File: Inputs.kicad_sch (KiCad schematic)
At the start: 6 parts, among them J23 Conn_01x04_Socket, J24 Conn_01x04_Socket, J25 Conn_01x04_Socket, J26 Conn_01x04_Socket, J27 Conn_01x02_Socket

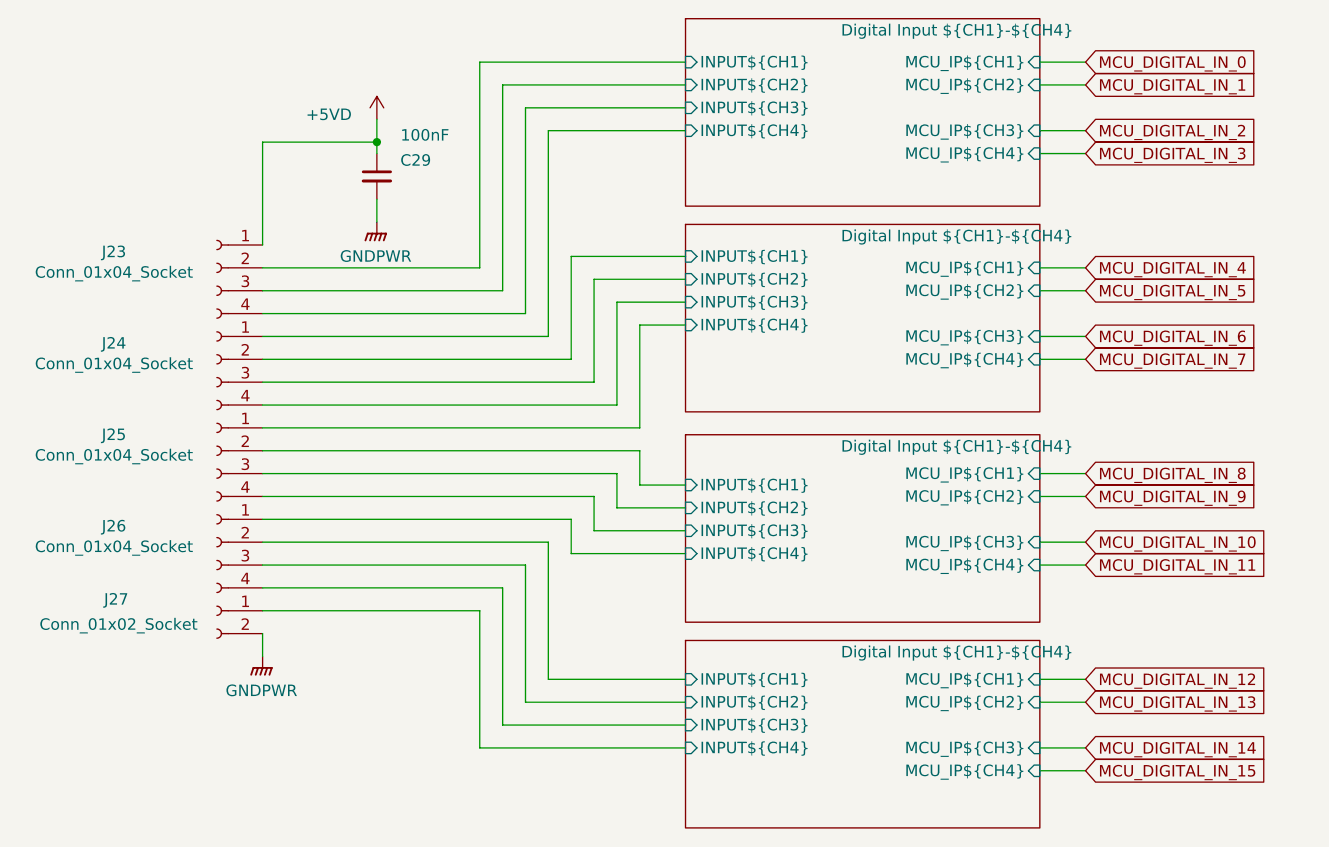
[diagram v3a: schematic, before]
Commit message: Added Analog inputs, updates to readme re powering board from external supply
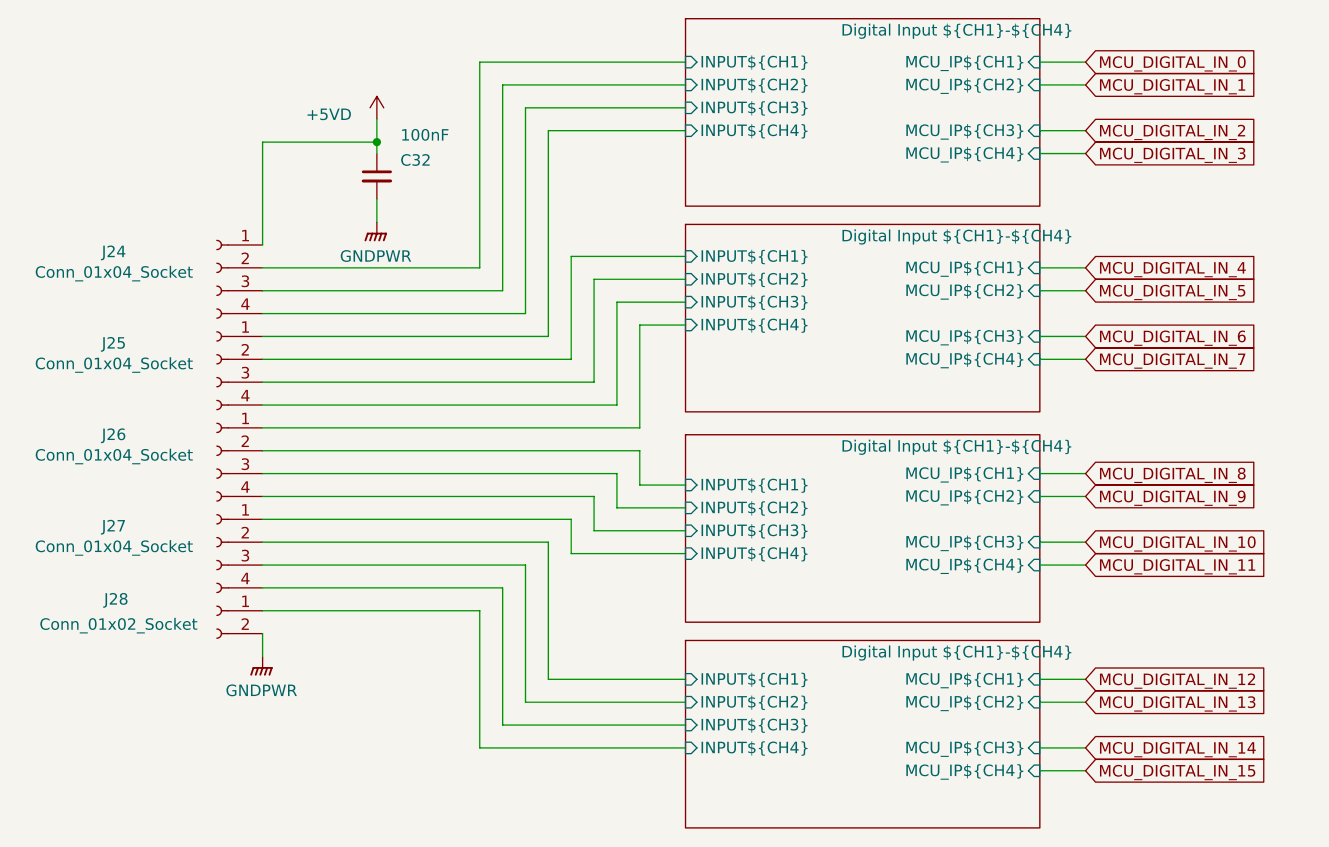
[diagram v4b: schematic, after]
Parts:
- renumbered C29 to C32, J23 to J24, J24 to J25, J25 to J26, J26 to J27, J27 to J28
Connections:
- net Digital Input ${CH1}-${CH4}/INPUT${CH1} is gone; now on net Digital Input ${CH1}-${CH4}/INPUT${CH1}: J25.2 (Pin_2)
- net Digital Input ${CH1}-${CH4}/INPUT${CH2} is gone; now on net Digital Input ${CH1}-${CH4}/INPUT${CH2}: J25.3 (Pin_3)
- net Digital Input ${CH1}-${CH4}/INPUT${CH3} is gone; now on net Digital Input ${CH1}-${CH4}/INPUT${CH3}: J25.4 (Pin_4)
- net Digital Input ${CH1}-${CH4}/INPUT${CH4} is gone; now on net Digital Input ${CH1}-${CH4}/INPUT${CH4}: J25.1 (Pin_1)
- net Digital Input ${CH1}-${CH4}/INPUT${CH1}: no longer J27.2 (Pin_2)
- net Digital Input ${CH1}-${CH4}/INPUT${CH2}: no longer J27.3 (Pin_3)
- net Digital Input ${CH1}-${CH4}/INPUT${CH3}: no longer J27.4 (Pin_4)
- net Digital Input ${CH1}-${CH4}/INPUT${CH4}: no longer J27.1 (Pin_1)
- new net Digital Input ${CH1}-${CH4}/INPUT${CH1}: J27.2 (Pin_2)
- new net Digital Input ${CH1}-${CH4}/INPUT${CH2}: J27.3 (Pin_3)
- new net Digital Input ${CH1}-${CH4}/INPUT${CH3}: J27.4 (Pin_4)
- new net Digital Input ${CH1}-${CH4}/INPUT${CH4}: J27.1 (Pin_1)
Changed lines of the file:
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@@
 		(on_board yes)
 		(dnp no)
-		(property "Reference" "J26"
+		(property "Reference" "J27"
 			(at 80.01 104.902 0)
 			(effects
@@
 			(project "Remora Nucleo F446ZE Hat"
 				(path "/5473abc6-7b93-43cc-a401-f691c4d7d7cf/181d5939-8311-41b3-8216-f7233e3a75eb"
-					(reference "J26")
+					(reference "J27")
 					(unit 1)
 				)
@@
 		(dnp no)
 		(fields_autoplaced yes)
-		(property "Reference" "#PWR0202"
+		(property "Reference" "#PWR0211"
 			(at 96.52 124.46 0)
 			(effects
@@
 			(project "Remora Nucleo F446ZE Hat"
 				(path "/5473abc6-7b93-43cc-a401-f691c4d7d7cf/181d5939-8311-41b3-8216-f7233e3a75eb"
-					(reference "#PWR0202")
+					(reference "#PWR0211")
 					(unit 1)
 				)
@@
 		(on_board yes)
 		(dnp no)
-		(property "Reference" "#PWR0203"
+		(property "Reference" "#PWR0212"
 			(at 109.22 63.5 0)
 			(effects
@@
 			(project "Remora Nucleo F446ZE Hat"
 				(path "/5473abc6-7b93-43cc-a401-f691c4d7d7cf/181d5939-8311-41b3-8216-f7233e3a75eb"
-					(reference "#PWR0203")
+					(reference "#PWR0212")
 					(unit 1)
 				)
@@
 		(on_board yes)
 		(dnp no)
-		(property "Reference" "J23"
+		(property "Reference" "J24"
 			(at 80.01 74.422 0)
 			(effects
@@
 			(project "Remora Nucleo F446ZE Hat"
 				(path "/5473abc6-7b93-43cc-a401-f691c4d7d7cf/181d5939-8311-41b3-8216-f7233e3a75eb"
-					(reference "J23")
+					(reference "J24")
 					(unit 1)
 				)
@@
 		(on_board yes)
 		(dnp no)
-		(property "Reference" "C29"
+		(property "Reference" "C32"
 			(at 113.538 64.262 0)
 			(effects
@@
 			(project "Remora Nucleo F446ZE Hat"
 				(path "/5473abc6-7b93-43cc-a401-f691c4d7d7cf/181d5939-8311-41b3-8216-f7233e3a75eb"
-					(reference "C29")
+					(reference "C32")
 					(unit 1)
 				)
@@
 		(dnp no)
 		(fields_autoplaced yes)
-		(property "Reference" "#PWR0204"
+		(property "Reference" "#PWR0213"
 			(at 109.22 76.2 0)
 			(effects
@@
 			(project "Remora Nucleo F446ZE Hat"
 				(path "/5473abc6-7b93-43cc-a401-f691c4d7d7cf/181d5939-8311-41b3-8216-f7233e3a75eb"
-					(reference "#PWR0204")
+					(reference "#PWR0213")
 					(unit 1)
 				)
@@
 		(on_board yes)
 		(dnp no)
-		(property "Reference" "J27"
+		(property "Reference" "J28"
 			(at 80.264 113.03 0)
 			(effects
@@
 			(project "Remora Nucleo F446ZE Hat"
 				(path "/5473abc6-7b93-43cc-a401-f691c4d7d7cf/181d5939-8311-41b3-8216-f7233e3a75eb"
-					(reference "J27")
+					(reference "J28")
 					(unit 1)
 				)
@@
 		(on_board yes)
 		(dnp no)
-		(property "Reference" "J25"
+		(property "Reference" "J26"
 			(at 80.01 94.742 0)
 			(effects
@@
 			(project "Remora Nucleo F446ZE Hat"
 				(path "/5473abc6-7b93-43cc-a401-f691c4d7d7cf/181d5939-8311-41b3-8216-f7233e3a75eb"
-					(reference "J25")
+					(reference "J26")
 					(unit 1)
 				)
@@
 		(on_board yes)
 		(dnp no)
-		(property "Reference" "J24"
+		(property "Reference" "J25"
 			(at 80.01 84.582 0)
 			(effects
@@
 			(project "Remora Nucleo F446ZE Hat"
 				(path "/5473abc6-7b93-43cc-a401-f691c4d7d7cf/181d5939-8311-41b3-8216-f7233e3a75eb"
-					(reference "J24")
-					(unit 1)
-				)
+					(reference "J25")
+					(unit 1)
+				)

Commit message: Added high speed encoder input circuitry. General tidy and updates to readme
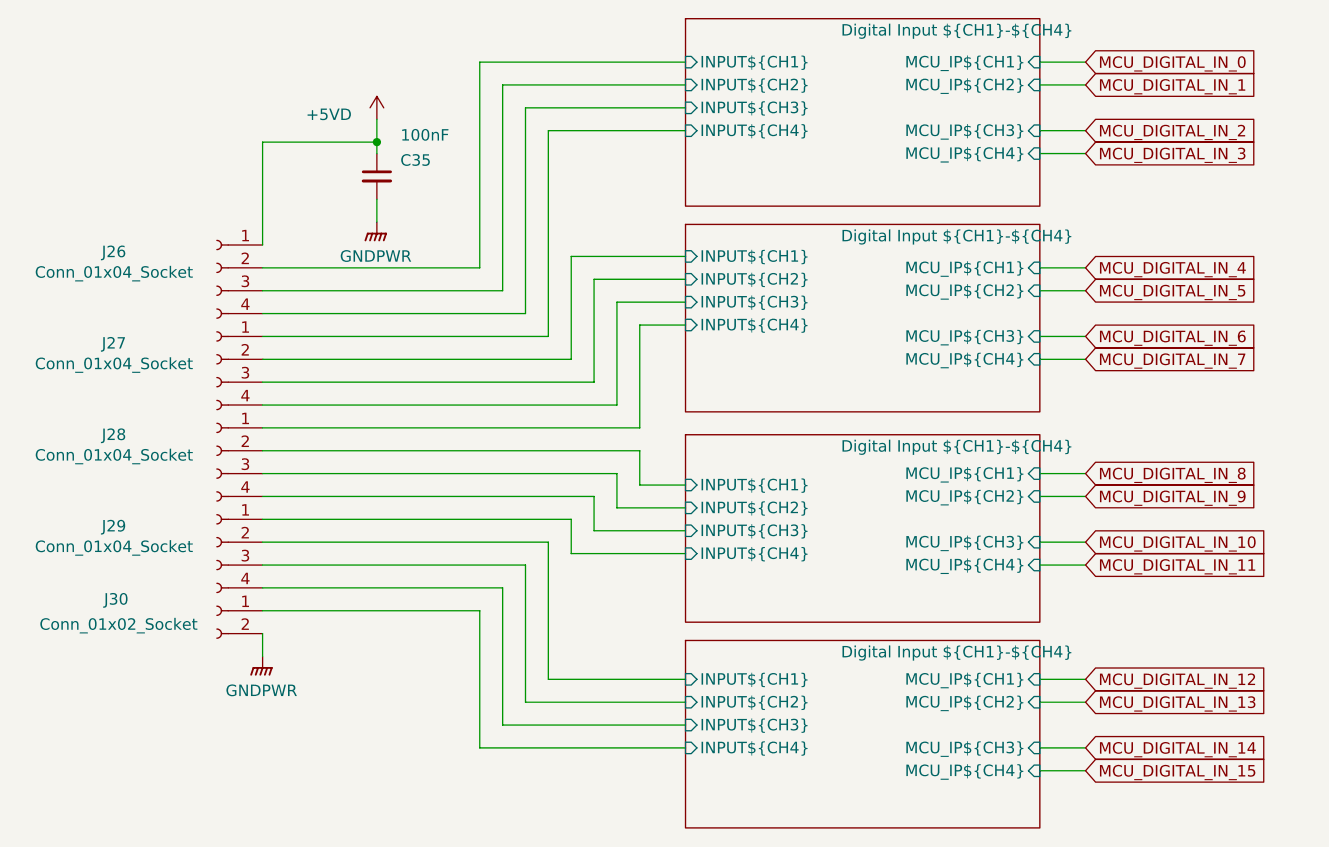
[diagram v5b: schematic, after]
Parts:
- renumbered C32 to C35, J24 to J26, J25 to J27, J26 to J28, J27 to J29, J28 to J30
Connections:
- net Digital Input ${CH1}-${CH4}/INPUT${CH1} is gone; now on net Digital Input ${CH1}-${CH4}/INPUT${CH1}: J27.2 (Pin_2)
- net Digital Input ${CH1}-${CH4}/INPUT${CH2} is gone; now on net Digital Input ${CH1}-${CH4}/INPUT${CH2}: J27.3 (Pin_3)
- net Digital Input ${CH1}-${CH4}/INPUT${CH3} is gone; now on net Digital Input ${CH1}-${CH4}/INPUT${CH3}: J27.4 (Pin_4)
- net Digital Input ${CH1}-${CH4}/INPUT${CH4} is gone; now on net Digital Input ${CH1}-${CH4}/INPUT${CH4}: J27.1 (Pin_1)
- net Digital Input ${CH1}-${CH4}/INPUT${CH1}: no longer J29.2 (Pin_2)
- net Digital Input ${CH1}-${CH4}/INPUT${CH2}: no longer J29.3 (Pin_3)
- net Digital Input ${CH1}-${CH4}/INPUT${CH3}: no longer J29.4 (Pin_4)
- net Digital Input ${CH1}-${CH4}/INPUT${CH4}: no longer J29.1 (Pin_1)
- new net Digital Input ${CH1}-${CH4}/INPUT${CH1}: J29.2 (Pin_2)
- new net Digital Input ${CH1}-${CH4}/INPUT${CH2}: J29.3 (Pin_3)
- new net Digital Input ${CH1}-${CH4}/INPUT${CH3}: J29.4 (Pin_4)
- new net Digital Input ${CH1}-${CH4}/INPUT${CH4}: J29.1 (Pin_1)
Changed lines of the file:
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@@
 		(on_board yes)
 		(dnp no)
-		(property "Reference" "J27"
+		(property "Reference" "J29"
 			(at 80.01 104.902 0)
 			(effects
@@
 			(project "Remora Nucleo F446ZE Hat"
 				(path "/5473abc6-7b93-43cc-a401-f691c4d7d7cf/181d5939-8311-41b3-8216-f7233e3a75eb"
-					(reference "J27")
+					(reference "J29")
 					(unit 1)
 				)
@@
 		(dnp no)
 		(fields_autoplaced yes)
-		(property "Reference" "#PWR0211"
+		(property "Reference" "#PWR0217"
 			(at 96.52 124.46 0)
 			(effects
@@
 			(project "Remora Nucleo F446ZE Hat"
 				(path "/5473abc6-7b93-43cc-a401-f691c4d7d7cf/181d5939-8311-41b3-8216-f7233e3a75eb"
-					(reference "#PWR0211")
+					(reference "#PWR0217")
 					(unit 1)
 				)
@@
 		(on_board yes)
 		(dnp no)
-		(property "Reference" "#PWR0212"
+		(property "Reference" "#PWR0218"
 			(at 109.22 63.5 0)
 			(effects
@@
 			(project "Remora Nucleo F446ZE Hat"
 				(path "/5473abc6-7b93-43cc-a401-f691c4d7d7cf/181d5939-8311-41b3-8216-f7233e3a75eb"
-					(reference "#PWR0212")
+					(reference "#PWR0218")
 					(unit 1)
 				)
@@
 		(on_board yes)
 		(dnp no)
-		(property "Reference" "J24"
+		(property "Reference" "J26"
 			(at 80.01 74.422 0)
 			(effects
@@
 			(project "Remora Nucleo F446ZE Hat"
 				(path "/5473abc6-7b93-43cc-a401-f691c4d7d7cf/181d5939-8311-41b3-8216-f7233e3a75eb"
-					(reference "J24")
+					(reference "J26")
 					(unit 1)
 				)
@@
 		(on_board yes)
 		(dnp no)
-		(property "Reference" "C32"
+		(property "Reference" "C35"
 			(at 113.538 64.262 0)
 			(effects
@@
 			(project "Remora Nucleo F446ZE Hat"
 				(path "/5473abc6-7b93-43cc-a401-f691c4d7d7cf/181d5939-8311-41b3-8216-f7233e3a75eb"
-					(reference "C32")
+					(reference "C35")
 					(unit 1)
 				)
@@
 		(dnp no)
 		(fields_autoplaced yes)
-		(property "Reference" "#PWR0213"
+		(property "Reference" "#PWR0219"
 			(at 109.22 76.2 0)
 			(effects
@@
 			(project "Remora Nucleo F446ZE Hat"
 				(path "/5473abc6-7b93-43cc-a401-f691c4d7d7cf/181d5939-8311-41b3-8216-f7233e3a75eb"
-					(reference "#PWR0213")
+					(reference "#PWR0219")
 					(unit 1)
 				)
@@
 		(on_board yes)
 		(dnp no)
-		(property "Reference" "J28"
+		(property "Reference" "J30"
 			(at 80.264 113.03 0)
 			(effects
@@
 			(project "Remora Nucleo F446ZE Hat"
 				(path "/5473abc6-7b93-43cc-a401-f691c4d7d7cf/181d5939-8311-41b3-8216-f7233e3a75eb"
-					(reference "J28")
+					(reference "J30")
 					(unit 1)
 				)
@@
 		(on_board yes)
 		(dnp no)
-		(property "Reference" "J26"
+		(property "Reference" "J28"
 			(at 80.01 94.742 0)
 			(effects
@@
 			(project "Remora Nucleo F446ZE Hat"
 				(path "/5473abc6-7b93-43cc-a401-f691c4d7d7cf/181d5939-8311-41b3-8216-f7233e3a75eb"
-					(reference "J26")
+					(reference "J28")
 					(unit 1)
 				)
@@
 		(on_board yes)
 		(dnp no)
-		(property "Reference" "J25"
+		(property "Reference" "J27"
 			(at 80.01 84.582 0)
 			(effects
@@
 			(project "Remora Nucleo F446ZE Hat"
 				(path "/5473abc6-7b93-43cc-a401-f691c4d7d7cf/181d5939-8311-41b3-8216-f7233e3a75eb"
-					(reference "J25")
-					(unit 1)
-				)
+					(reference "J27")
+					(unit 1)
+				)

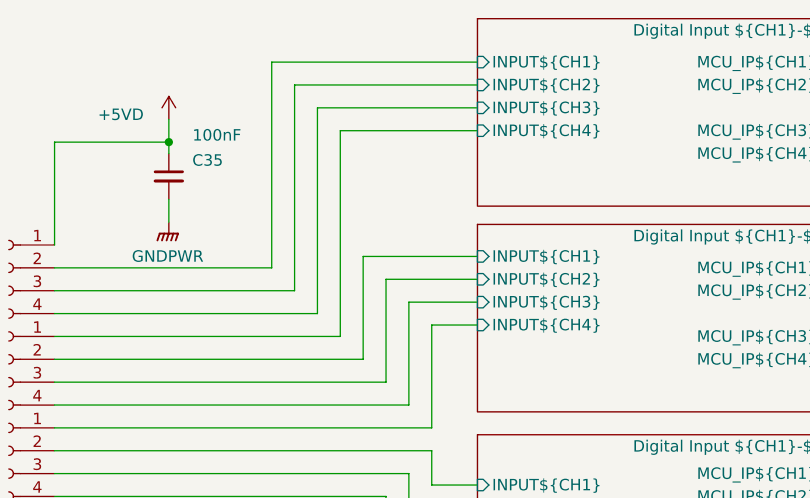
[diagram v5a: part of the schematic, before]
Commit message: Layout for stepper drivers and digital inputs
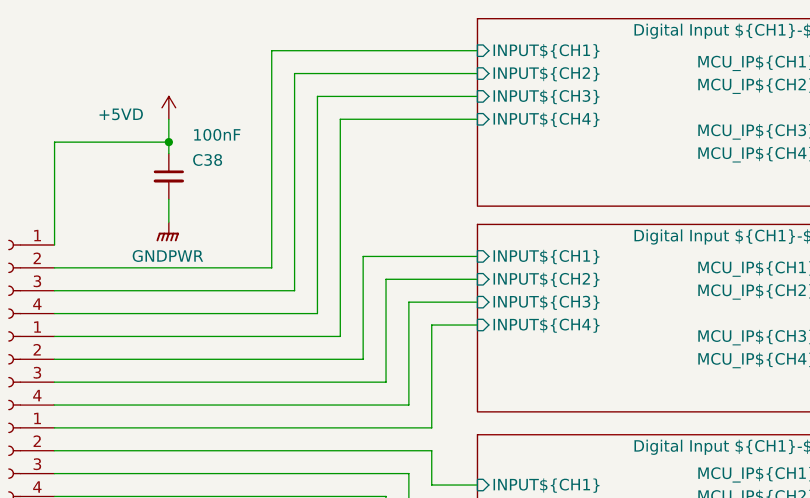
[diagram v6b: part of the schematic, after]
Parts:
- renumbered C35 to C38
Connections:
- net Digital Input ${CH1}-${CH4}/INPUT${CH1} is gone; now on net Digital Input ${CH1}-${CH4}/INPUT${CH1}: J27.2 (Pin_2)
- net Digital Input ${CH1}-${CH4}/INPUT${CH2} is gone; now on net Digital Input ${CH1}-${CH4}/INPUT${CH2}: J27.3 (Pin_3)
- net Digital Input ${CH1}-${CH4}/INPUT${CH3} is gone; now on net Digital Input ${CH1}-${CH4}/INPUT${CH3}: J27.4 (Pin_4)
- net Digital Input ${CH1}-${CH4}/INPUT${CH4} is gone; now on net Digital Input ${CH1}-${CH4}/INPUT${CH4}: J27.1 (Pin_1)
- net Digital Input ${CH1}-${CH4}/INPUT${CH1}: no longer J29.2 (Pin_2)
- net Digital Input ${CH1}-${CH4}/INPUT${CH2}: no longer J29.3 (Pin_3)
- net Digital Input ${CH1}-${CH4}/INPUT${CH3}: no longer J29.4 (Pin_4)
- net Digital Input ${CH1}-${CH4}/INPUT${CH4}: no longer J29.1 (Pin_1)
- new net Digital Input ${CH1}-${CH4}/INPUT${CH1}: J29.2 (Pin_2)
- new net Digital Input ${CH1}-${CH4}/INPUT${CH2}: J29.3 (Pin_3)
- new net Digital Input ${CH1}-${CH4}/INPUT${CH3}: J29.4 (Pin_4)
- new net Digital Input ${CH1}-${CH4}/INPUT${CH4}: J29.1 (Pin_1)
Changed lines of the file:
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@@
 	(wire
 		(pts
-			(xy 120.65 53.34) (xy 143.51 53.34)
+			(xy 120.65 52.07) (xy 143.51 52.07)
 		)
 		(stroke
@@
 	(wire
 		(pts
-			(xy 123.19 55.88) (xy 143.51 55.88)
+			(xy 123.19 54.61) (xy 143.51 54.61)
 		)
 		(stroke
@@
 	(wire
 		(pts
-			(xy 120.65 53.34) (xy 120.65 76.2)
+			(xy 120.65 52.07) (xy 120.65 76.2)
 		)
 		(stroke
@@
 	(wire
 		(pts
-			(xy 125.73 58.42) (xy 143.51 58.42)
+			(xy 125.73 57.15) (xy 143.51 57.15)
 		)
 		(stroke
@@
 	(wire
 		(pts
-			(xy 128.27 60.96) (xy 128.27 83.82)
+			(xy 128.27 59.69) (xy 128.27 83.82)
 		)
 		(stroke
@@
 	(wire
 		(pts
-			(xy 125.73 58.42) (xy 125.73 81.28)
+			(xy 125.73 57.15) (xy 125.73 81.28)
 		)
 		(stroke
@@
 	(wire
 		(pts
-			(xy 123.19 55.88) (xy 123.19 78.74)
-		)
-		(stroke
-			(width 0)
-			(type default)
-		)
-	)
-	(wire
-		(pts
-			(xy 128.27 60.96) (xy 143.51 60.96)
+			(xy 123.19 54.61) (xy 123.19 78.74)
+		)
+		(stroke
+			(width 0)
+			(type default)
+		)
+	)
+	(wire
+		(pts
+			(xy 128.27 59.69) (xy 143.51 59.69)
 		)
 		(stroke
@@
 		(dnp no)
 		(fields_autoplaced yes)
-		(property "Reference" "#PWR0217"
+		(property "Reference" "#PWR0228"
 			(at 96.52 124.46 0)
 			(effects
@@
 			(project "Remora Nucleo F446ZE Hat"
 				(path "/5473abc6-7b93-43cc-a401-f691c4d7d7cf/181d5939-8311-41b3-8216-f7233e3a75eb"
-					(reference "#PWR0217")
+					(reference "#PWR0228")
 					(unit 1)
 				)
@@
 		(on_board yes)
 		(dnp no)
-		(property "Reference" "#PWR0218"
+		(property "Reference" "#PWR0229"
 			(at 109.22 63.5 0)
 			(effects
@@
 			(project "Remora Nucleo F446ZE Hat"
 				(path "/5473abc6-7b93-43cc-a401-f691c4d7d7cf/181d5939-8311-41b3-8216-f7233e3a75eb"
-					(reference "#PWR0218")
+					(reference "#PWR0229")
 					(unit 1)
 				)
@@
 		(on_board yes)
 		(dnp no)
-		(property "Reference" "C35"
+		(property "Reference" "C38"
 			(at 113.538 64.262 0)
 			(effects
@@
 			(project "Remora Nucleo F446ZE Hat"
 				(path "/5473abc6-7b93-43cc-a401-f691c4d7d7cf/181d5939-8311-41b3-8216-f7233e3a75eb"
-					(reference "C35")
+					(reference "C38")
 					(unit 1)
 				)
@@
 		(dnp no)
 		(fields_autoplaced yes)
-		(property "Reference" "#PWR0219"
+		(property "Reference" "#PWR0230"
 			(at 109.22 76.2 0)
 			(effects
@@
 			(project "Remora Nucleo F446ZE Hat"
 				(path "/5473abc6-7b93-43cc-a401-f691c4d7d7cf/181d5939-8311-41b3-8216-f7233e3a75eb"
-					(reference "#PWR0219")
+					(reference "#PWR0230")
 					(unit 1)
 				)
@@
 		)
 		(pin "INPUT${CH1}" input
-			(at 143.51 53.34 180)
+			(at 143.51 52.07 180)
 			(effects
 				(font
@@
 		)
 		(pin "INPUT${CH2}" input
-			(at 143.51 55.88 180)
+			(at 143.51 54.61 180)
 			(effects
 				(font
@@
 		)
 		(pin "INPUT${CH3}" input
-			(at 143.51 58.42 180)
+			(at 143.51 57.15 180)
 			(effects
 				(font
@@
 		)
 		(pin "INPUT${CH4}" input
-			(at 143.51 60.96 180)
+			(at 143.51 59.69 180)
 			(effects
 				(font
@@
 			(project "Remora Nucleo F446ZE Hat"
 				(path "/5473abc6-7b93-43cc-a401-f691c4d7d7cf/181d5939-8311-41b3-8216-f7233e3a75eb"
-					(page "20")
-				)
-			)
+					(page "9")
+				)
+			)
